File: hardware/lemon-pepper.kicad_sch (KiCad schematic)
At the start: 36 parts, among them J101 INPUT, M101 MOT

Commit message: finish layout and prod files
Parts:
- removed C109, C110, C111, C112: 100uF, Capacitor_SMD:CP_Elec_10x10.5, symbol Device:C_Polarized_Small
- removed TP101: DIR/CANH, TestPoint:TestPoint_Pad_D1.0mm, symbol Connector:TestPoint
- removed TP102: STEP/CANL, TestPoint:TestPoint_Pad_D1.0mm, symbol Connector:TestPoint
- removed TP103: USBP, TestPoint:TestPoint_Pad_D1.0mm, symbol Connector:TestPoint
- removed TP104: USBM, TestPoint:TestPoint_Pad_D1.0mm, symbol Connector:TestPoint
- removed TP105: U_SENS, TestPoint:TestPoint_Pad_D1.0mm, symbol Connector:TestPoint
- removed TP106: A, TestPoint:TestPoint_Pad_D1.0mm, symbol Connector:TestPoint
- removed TP107: B, TestPoint:TestPoint_Pad_D1.0mm, symbol Connector:TestPoint
- removed TP108: V_SENS, TestPoint:TestPoint_Pad_D1.0mm, symbol Connector:TestPoint
- removed TP109: Z, TestPoint:TestPoint_Pad_D1.0mm, symbol Connector:TestPoint
- removed TP110: W_SENS, TestPoint:TestPoint_Pad_D1.0mm, symbol Connector:TestPoint
- removed TP111: W, TestPoint:TestPoint_Pad_D1.0mm, symbol Connector:TestPoint
- removed TP112: V, TestPoint:TestPoint_Pad_D1.0mm, symbol Connector:TestPoint
- removed TP113: U, TestPoint:TestPoint_Pad_D1.0mm, symbol Connector:TestPoint
- added R602, R603: 0R, Resistor_SMD:R_0402_1005Metric, symbol Device:R_Small_US
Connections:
- net GND: now also R602.2, R603.1; no longer R602.1, R603.2
- net mcu/CANH: now also R603.2
- net mcu/CANL: now also R602.1
- net usb/UCPD_CC1: now also R602.1; no longer R603.1
- net usb/UCPD_CC2: now also R603.2; no longer R602.2
- new net mcu/DIR: R602.2
- new net mcu/STEP: R603.1
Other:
- moved on the sheet: C101, C102, C103, C104, C105, C106, C107, C108, D101, J101, JP101, R103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

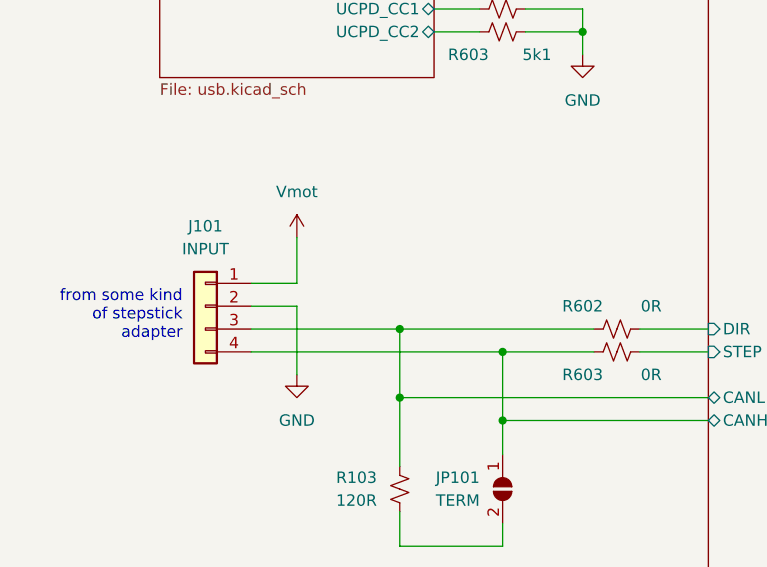
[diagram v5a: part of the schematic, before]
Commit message: clean up ERC in schematic
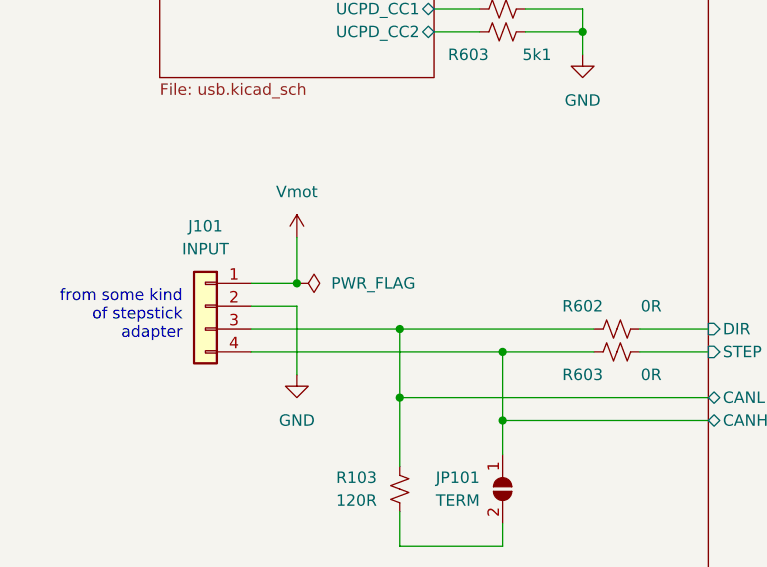
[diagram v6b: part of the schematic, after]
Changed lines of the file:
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@@
   (junction (at 248.92 76.2) (diameter 0) (color 0 0 0 0)
+  )
+  (junction (at 46.99 87.63) (diameter 0) (color 0 0 0 0)
   )
   (junction (at 58.42 92.71) (diameter 0) (color 0 0 0 0)
@@
         )
       )
+    )
+  )
+  (symbol (lib_id "power:PWR_FLAG") (at 46.99 87.63 270) (unit 1)
+    (in_bom yes) (on_board yes) (dnp no) (fields_autoplaced)
+    (property "Reference" "#FLG0101" (at 48.895 87.63 0)
+      (effects (font (size 1.27 1.27)) hide)
+    )
+    (property "Value" "PWR_FLAG" (at 50.8 87.63 90)
+      (effects (font (size 1.27 1.27)) (justify left))
+    )
+    (property "Footprint" "" (at 46.99 87.63 0)
+      (effects (font (size 1.27 1.27)) hide)
+    )
+    (property "Datasheet" "~" (at 46.99 87.63 0)
+      (effects (font (size 1.27 1.27)) hide)
+    )
+    (pin "1")
+    (instances
+      (project "lemon-pepper"
+        (path "/0306e2fa-4433-4288-91d9-65a3484207ad"
+          (reference "#FLG0101") (unit 1)
+        )
+      )

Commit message: bringup changes
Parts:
- JP101: footprint Jumper:SolderJumper-2_P1.3mm_Open_RoundedPad1.0x1.5mm -> Resistor_SMD:R_0402_1005Metric; now not fitted
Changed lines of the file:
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@@
   )
   (symbol (lib_id "Jumper:SolderJumper_2_Open") (at 69.85 110.49 90) (mirror x) (unit 1)
-    (in_bom no) (on_board yes) (dnp no)
+    (in_bom no) (on_board yes) (dnp yes)
     (property "Reference" "JP101" (at 67.31 109.22 90)
       (effects (font (size 1.27 1.27)) (justify left))
@@
       (effects (font (size 1.27 1.27)) (justify left))
     )
-    (property "Footprint" "Jumper:SolderJumper-2_P1.3mm_Open_RoundedPad1.0x1.5mm" (at 69.85 110.49 0)
+    (property "Footprint" "Resistor_SMD:R_0402_1005Metric" (at 69.85 110.49 0)
       (effects (font (size 1.27 1.27)) hide)
     )

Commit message: update pcb layout
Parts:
- added C109: 10u, Capacitor_SMD:C_0805_2012Metric, symbol Device:C_Small
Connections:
- net GND: now also C109.1
- net Vmot: now also C109.2
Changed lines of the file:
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@@
   (junction (at 78.74 59.69) (diameter 0) (color 0 0 0 0)
   )
+  (junction (at 147.32 177.8) (diameter 0) (color 0 0 0 0)
+  )
   (junction (at 69.85 95.25) (diameter 0) (color 0 0 0 0)
   )
@@
   (junction (at 69.85 102.87) (diameter 0) (color 0 0 0 0)
   )
+  (junction (at 137.16 186.69) (diameter 0) (color 0 0 0 0)
+  )
   (junction (at 132.08 170.18) (diameter 0) (color 0 0 0 0)
   )
@@
     (stroke (width 0) (type default))
   )
+  (wire (pts (xy 147.32 186.69) (xy 147.32 185.42))
+    (stroke (width 0) (type default))
+  )
   (wire (pts (xy 135.89 62.23) (xy 167.64 62.23))
     (stroke (width 0) (type default))
   )
+  (wire (pts (xy 147.32 180.34) (xy 147.32 177.8))
+    (stroke (width 0) (type default))
+  )
   (wire (pts (xy 271.78 138.43) (xy 271.78 144.78))
     (stroke (width 0) (type default))
@@
   )
   (wire (pts (xy 240.03 57.15) (xy 240.03 71.12))
+    (stroke (width 0) (type default))
+  )
+  (wire (pts (xy 137.16 186.69) (xy 147.32 186.69))
     (stroke (width 0) (type default))
   )
@@
     (stroke (width 0) (type dash))
   )
+  (wire (pts (xy 147.32 177.8) (xy 157.48 177.8))
+    (stroke (width 0) (type default))
+  )
   (wire (pts (xy 41.91 92.71) (xy 58.42 92.71))
     (stroke (width 0) (type default))
@@
     (stroke (width 0) (type default))
   )
-  (wire (pts (xy 149.86 177.8) (xy 149.86 180.34))
+  (wire (pts (xy 157.48 177.8) (xy 157.48 180.34))
     (stroke (width 0) (type default))
   )
@@
     (stroke (width 0) (type default))
   )
-  (wire (pts (xy 142.24 177.8) (xy 149.86 177.8))
+  (wire (pts (xy 142.24 177.8) (xy 147.32 177.8))
     (stroke (width 0) (type default))
   )
@@
     )
   )
-  (symbol (lib_id "power:GND") (at 149.86 180.34 0) (unit 1)
+  (symbol (lib_id "power:GND") (at 157.48 180.34 0) (unit 1)
     (in_bom yes) (on_board yes) (dnp no) (fields_autoplaced)
-    (property "Reference" "#PWR0105" (at 149.86 186.69 0)
-      (effects (font (size 1.27 1.27)) hide)
-    )
-    (property "Value" "GND" (at 149.86 185.42 0)
-      (effects (font (size 1.27 1.27)))
-    )
-    (property "Footprint" "" (at 149.86 180.34 0)
-      (effects (font (size 1.27 1.27)) hide)
-    )
-    (property "Datasheet" "" (at 149.86 180.34 0)
+    (property "Reference" "#PWR0105" (at 157.48 186.69 0)
+      (effects (font (size 1.27 1.27)) hide)
+    )
+    (property "Value" "GND" (at 157.48 185.42 0)
+      (effects (font (size 1.27 1.27)))
+    )
+    (property "Footprint" "" (at 157.48 180.34 0)
+      (effects (font (size 1.27 1.27)) hide)
+    )
+    (property "Datasheet" "" (at 157.48 180.34 0)
       (effects (font (size 1.27 1.27)) hide)
     )
@@
         )
       )
+    )
+  )
+  (symbol (lib_id "Device:C_Small") (at 147.32 182.88 0) (unit 1)
+    (in_bom yes) (on_board yes) (dnp no)
+    (property "Reference" "C109" (at 149.86 181.6163 0)
+      (effects (font (size 1.27 1.27)) (justify left))
+    )
+    (property "Value" "10u" (at 149.86 184.1563 0)
+      (effects (font (size 1.27 1.27)) (justify left))
+    )
+    (property "Footprint" "Capacitor_SMD:C_0805_2012Metric" (at 147.32 182.88 0)
+      (effects (font (size 1.27 1.27)) hide)
+    )
+    (property "Datasheet" "~" (at 147.32 182.88 0)
+      (effects (font (size 1.27 1.27)) hide)
+    )
+    (property "LCSC Part" "C440198" (at 147.32 182.88 0)
+      (effects (font (size 1.27 1.27)) hide)
+    )
+    (pin "1")
+    (pin "2")
+    (instances
+      (project "lemon-pepper"
+        (path "/0306e2fa-4433-4288-91d9-65a3484207ad"
+          (reference "C109") (unit 1)
+        )
+      )
